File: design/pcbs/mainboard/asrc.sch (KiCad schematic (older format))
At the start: 18 parts, among them J5 Conn_01x03, U1 TPS79318-EP, U2 SRC4392

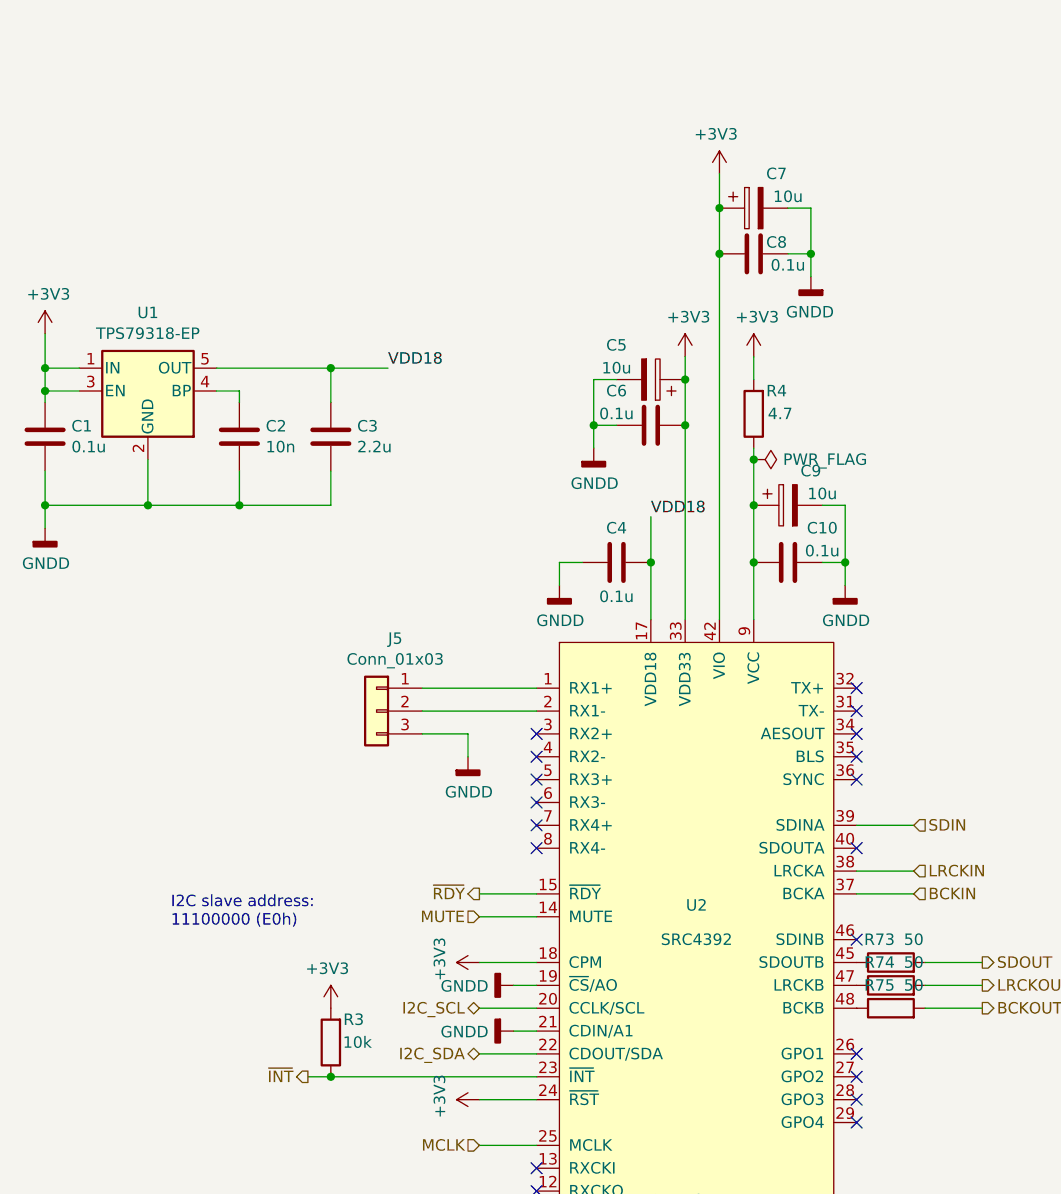
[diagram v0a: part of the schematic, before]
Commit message: Renumbered footprints to follow board position.
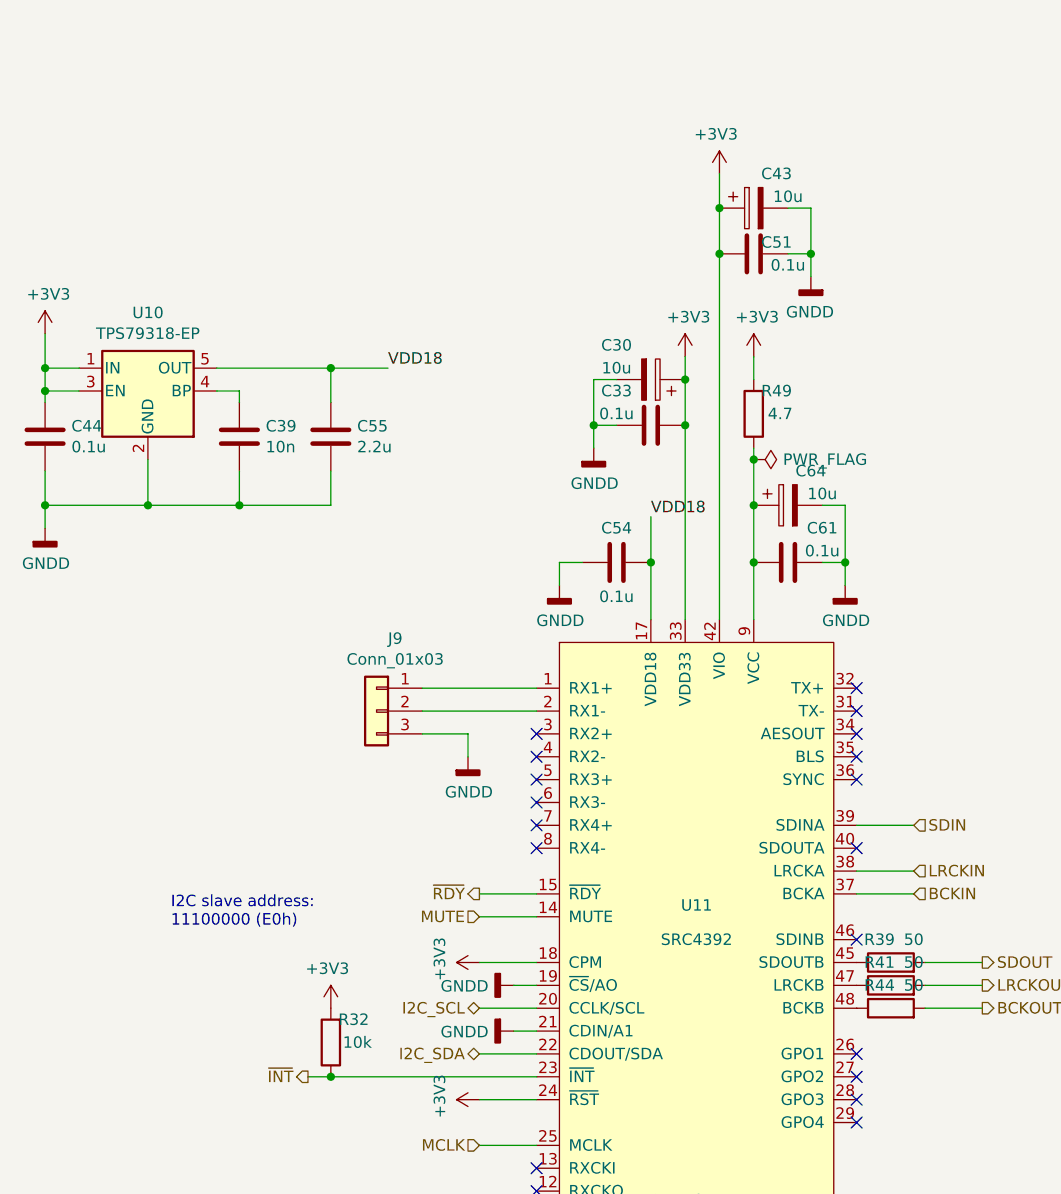
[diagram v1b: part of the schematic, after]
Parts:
- renumbered C5 to C30, C6 to C33, C2 to C39, C7 to C43, C1 to C44, C8 to C51, C4 to C54, C3 to C55, C10 to C61, C9 to C64, J5 to J9, R3 to R32, R73 to R39, R74 to R41, R75 to R44, R4 to R49, U1 to U10, U2 to U11
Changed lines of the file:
@@
 $EndDescr
 $Comp
-L dac:SRC4392 U2
+L dac:SRC4392 U11
 U 1 1 5EC7924C
 P 4700 4750
-F 0 "U2" H 4700 4900 50  0000 C CNN
+F 0 "U11" H 4700 4900 50  0000 C CNN
 F 1 "SRC4392" H 4700 4750 50  0000 C CNN
 F 2 "Package_QFP:TQFP-48_7x7mm_P0.5mm" H 4750 6100 50  0001 C CNN
@@
 $EndBitmap
 $Comp
-L Regulator_Linear:TPS79318-EP U1
+L Regulator_Linear:TPS79318-EP U10
 U 1 1 5EC6440E
 P 2300 2350
-F 0 "U1" H 2300 2692 50  0000 C CNN
+F 0 "U10" H 2300 2692 50  0000 C CNN
 F 1 "TPS79318-EP" H 2300 2601 50  0000 C CNN
 F 2 "Package_TO_SOT_SMD:SOT-23-5" H 2300 2675 50  0001 C CIN
@@
 $EndComp
 $Comp
-L Device:C C1
+L Device:C C44
 U 1 1 5EC64F1A
 P 1850 2550
-F 0 "C1" H 1965 2596 50  0000 L CNN
+F 0 "C44" H 1965 2596 50  0000 L CNN
 F 1 "0.1u" H 1965 2505 50  0000 L CNN
 F 2 "Capacitor_SMD:C_0603_1608Metric" H 1888 2400 50  0001 C CNN
@@
 $EndComp
 $Comp
-L Device:C C2
+L Device:C C39
 U 1 1 5EC677C7
 P 2700 2550
-F 0 "C2" H 2815 2596 50  0000 L CNN
+F 0 "C39" H 2815 2596 50  0000 L CNN
 F 1 "10n" H 2815 2505 50  0000 L CNN
 F 2 "Capacitor_SMD:C_0402_1005Metric" H 2738 2400 50  0001 C CNN
@@
 $EndComp
 $Comp
-L Device:C C3
+L Device:C C55
 U 1 1 5EC680BF
 P 3100 2550
-F 0 "C3" H 3215 2596 50  0000 L CNN
+F 0 "C55" H 3215 2596 50  0000 L CNN
 F 1 "2.2u" H 3215 2505 50  0000 L CNN
 F 2 "Capacitor_SMD:C_0603_1608Metric" H 3138 2400 50  0001 C CNN
@@
 Connection ~ 1850 2250
 $Comp
-L Device:C C10
+L Device:C C61
 U 1 1 5EC754F8
 P 5100 3100
-F 0 "C10" V 4950 3250 50  0000 C CNN
+F 0 "C61" V 4950 3250 50  0000 C CNN
 F 1 "0.1u" V 5050 3250 50  0000 C CNN
 F 2 "Capacitor_SMD:C_0603_1608Metric" H 5138 2950 50  0001 C CNN
@@
 $EndComp
 $Comp
-L Device:C C4
+L Device:C C54
 U 1 1 5EC782F3
 P 4350 3100
-F 0 "C4" V 4200 3100 50  0000 C CNN
+F 0 "C54" V 4200 3100 50  0000 C CNN
 F 1 "0.1u" V 4500 3100 50  0000 C CNN
 F 2 "Capacitor_SMD:C_0603_1608Metric" H 4388 2950 50  0001 C CNN
@@
 $EndComp
 $Comp
-L Device:CP C7
+L Device:CP C43
 U 1 1 5EC93F8F
 P 4950 1550
-F 0 "C7" V 4800 1450 50  0000 C CNN
+F 0 "C43" V 4800 1450 50  0000 C CNN
 F 1 "10u" V 4900 1400 50  0000 C CNN
 F 2 "Capacitor_Tantalum_SMD:CP_EIA-3216-18_Kemet-A" H 4988 1400 50  0001 C CNN
@@
 	4800 1550 4800 1750
 $Comp
-L Device:C C8
+L Device:C C51
 U 1 1 5EC944E8
 P 4950 1750
-F 0 "C8" V 4900 1650 50  0000 C CNN
+F 0 "C51" V 4900 1650 50  0000 C CNN
 F 1 "0.1u" V 5000 1600 50  0000 C CNN
 F 2 "Capacitor_SMD:C_0603_1608Metric" H 4988 1600 50  0001 C CNN
@@
 	4650 3350 4650 2500
 $Comp
-L Device:C C6
+L Device:C C33
 U 1 1 5ECB3139
 P 4500 2500
-F 0 "C6" V 4350 2350 50  0000 C CNN
+F 0 "C33" V 4350 2350 50  0000 C CNN
 F 1 "0.1u" V 4450 2350 50  0000 C CNN
 F 2 "Capacitor_SMD:C_0603_1608Metric" H 4538 2350 50  0001 C CNN
@@
 	4650 2200 4650 2300
 $Comp
-L Device:CP C5
+L Device:CP C30
 U 1 1 5ECEFB6A
 P 4500 2300
-F 0 "C5" V 4650 2150 50  0000 C CNN
+F 0 "C30" V 4650 2150 50  0000 C CNN
 F 1 "10u" V 4550 2150 50  0000 C CNN
 F 2 "Capacitor_Tantalum_SMD:CP_EIA-3216-18_Kemet-A" H 4538 2150 50  0001 C CNN
@@
 	4650 2300 4650 2500
 $Comp
-L Device:CP C9
+L Device:CP C64
 U 1 1 5ECF148F
 P 5100 2850
-F 0 "C9" V 4950 2750 50  0000 C CNN
+F 0 "C64" V 4950 2750 50  0000 C CNN
 F 1 "10u" V 5050 2700 50  0000 C CNN
 F 2 "Capacitor_Tantalum_SMD:CP_EIA-3216-18_Kemet-A" H 5138 2700 50  0001 C CNN
@@
 P 3100 5200
 AR Path="/5ECDE056" Ref="R?"  Part="1"
-AR Path="/5EC77FFA/5ECDE056" Ref="R3"  Part="1"
-F 0 "R3" H 3000 5100 50  0000 C CNN
+AR Path="/5EC77FFA/5ECDE056" Ref="R32"  Part="1"
+F 0 "R32" H 3000 5100 50  0000 C CNN
 F 1 "10k" H 2984 5200 50  0000 C CNN
 F 2 "Resistor_SMD:R_0402_1005Metric" V 3030 5200 50  0001 C CNN
@@
 P 4950 2450
 AR Path="/5ED97A18" Ref="R?"  Part="1"
-AR Path="/5EC77FFA/5ED97A18" Ref="R4"  Part="1"
-F 0 "R4" H 4850 2350 50  0000 C CNN
+AR Path="/5EC77FFA/5ED97A18" Ref="R49"  Part="1"
+F 0 "R49" H 4850 2350 50  0000 C CNN
 F 1 "4.7" H 4834 2450 50  0000 C CNN
 F 2 "Resistor_SMD:R_0603_1608Metric" V 4880 2450 50  0001 C CNN
@@
 NoConn ~ 4000 4350
 $Comp
-L Connector_Generic:Conn_01x03 J5
+L Connector_Generic:Conn_01x03 J9
 U 1 1 5EDD40DB
 P 3300 3750
-F 0 "J5" H 3218 4067 50  0000 C CNN
+F 0 "J9" H 3218 4067 50  0000 C CNN
 F 1 "Conn_01x03" H 3218 3976 50  0000 C CNN
 F 2 "Connector_PinHeader_2.54mm:PinHeader_1x03_P2.54mm_Vertical" H 3300 3750 50  0001 C CNN
@@
 P 5550 4850
 AR Path="/5EEA869D" Ref="R?"  Part="1"
-AR Path="/5EC77FFA/5EEA869D" Ref="R73"  Part="1"
-F 0 "R73" V 5650 4900 50  0000 C CNN
+AR Path="/5EC77FFA/5EEA869D" Ref="R39"  Part="1"
+F 0 "R39" V 5650 4900 50  0000 C CNN
 F 1 "50" V 5650 4750 50  0000 C CNN
 F 2 "Resistor_SMD:R_0402_1005Metric" V 5480 4850 50  0001 C CNN
@@
 P 5550 4950
 AR Path="/5EEAFFEA" Ref="R?"  Part="1"
-AR Path="/5EC77FFA/5EEAFFEA" Ref="R74"  Part="1"
-F 0 "R74" V 5650 5000 50  0000 C CNN
+AR Path="/5EC77FFA/5EEAFFEA" Ref="R41"  Part="1"
+F 0 "R41" V 5650 5000 50  0000 C CNN
 F 1 "50" V 5650 4850 50  0000 C CNN
 F 2 "Resistor_SMD:R_0402_1005Metric" V 5480 4950 50  0001 C CNN
@@
 P 5550 5050
 AR Path="/5EEB02AB" Ref="R?"  Part="1"
-AR Path="/5EC77FFA/5EEB02AB" Ref="R75"  Part="1"
-F 0 "R75" V 5650 5100 50  0000 C CNN
+AR Path="/5EC77FFA/5EEB02AB" Ref="R44"  Part="1"
+F 0 "R44" V 5650 5100 50  0000 C CNN
 F 1 "50" V 5650 4950 50  0000 C CNN
 F 2 "Resistor_SMD:R_0402_1005Metric" V 5480 5050 50  0001 C CNN

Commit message: Fixed title blocks. Added fab outputs.
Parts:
- U10: LCSC (none) -> C7102
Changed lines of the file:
@@
 encoding utf-8
 Sheet 2 10
-Title ""
-Date ""
-Rev ""
-Comp ""
-Comment1 ""
-Comment2 ""
+Title "DAC1 Main board"
+Date "2020-06-27"
+Rev "1.0.0"
+Comp "© Mark Pinese 2020"
+Comment1 "To view a copy of this license, visit https://creativecommons.org/licenses/by/4.0"
+Comment2 "This work is licensed under CC BY 4.0."
 Comment3 ""
 Comment4 ""
@@
 F 4 "296-12155-1-ND" H 2300 2350 50  0001 C CNN "DigiKey"
 F 5 "Yes" H 2300 2350 50  0001 C CNN "Done"
+F 6 "C7102" H 2300 2350 50  0001 C CNN "LCSC"
 	1    2300 2350
 	1    0    0    -1

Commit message: Misc updates
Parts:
- R39, R41, R44: value 50 -> 10; LCSC C25082 -> C25077
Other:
- moved on the sheet: R39, R41, R44
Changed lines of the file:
@@
 $EndComp
 Wire Wire Line
-	5950 5050 5700 5050
+	6100 5050 5850 5050
 Wire Wire Line
-	5700 4950 5950 4950
-Text HLabel 5950 5050 2    50   Output ~ 0
+	5850 4950 6100 4950
+Text HLabel 6100 5050 2    50   Output ~ 0
 BCKOUT
-Text HLabel 5950 4950 2    50   Output ~ 0
+Text HLabel 6100 4950 2    50   Output ~ 0
 LRCKOUT
 Wire Wire Line
-	5700 4850 5950 4850
-Text HLabel 5950 4850 2    50   Output ~ 0
+	5850 4850 6100 4850
+Text HLabel 6100 4850 2    50   Output ~ 0
 SDOUT
 $Comp
 L Device:R R?
 U 1 1 5EEA869D
-P 5550 4850
+P 5700 4850
 AR Path="/5EEA869D" Ref="R?"  Part="1"
 AR Path="/5EC77FFA/5EEA869D" Ref="R39"  Part="1"
-F 0 "R39" V 5650 4900 50  0000 C CNN
-F 1 "50" V 5650 4750 50  0000 C CNN
-F 2 "Resistor_SMD:R_0402_1005Metric" V 5480 4850 50  0001 C CNN
-F 3 "https://datasheet.lcsc.com/szlcsc/Uniroyal-Elec-0402WGF1500TCE_C25082.pdf" H 5550 4850 50  0001 C CNN
-F 4 "C25082" H 5550 4850 50  0001 C CNN "LCSC"
-F 5 "Yes" H 5550 4850 50  0001 C CNN "Done"
-F 6 "Termination" H 5550 4850 50  0001 C CNN "Function"
-	1    5550 4850
+F 0 "R39" V 5750 5050 50  0000 C CNN
+F 1 "10" V 5700 4850 50  0000 C CNN
+F 2 "Resistor_SMD:R_0402_1005Metric" V 5630 4850 50  0001 C CNN
+F 3 "Uniroyal-Elec-0402WGF100JTCE_C25077.pdf" H 5700 4850 50  0001 C CNN
+F 4 "C25077" H 5700 4850 50  0001 C CNN "LCSC"
+F 5 "Yes" H 5700 4850 50  0001 C CNN "Done"
+F 6 "Termination" H 5700 4850 50  0001 C CNN "Function"
+	1    5700 4850
 	0    -1   -1   0
 $EndComp
@@
 L Device:R R?
 U 1 1 5EEAFFEA
-P 5550 4950
+P 5700 4950
 AR Path="/5EEAFFEA" Ref="R?"  Part="1"
 AR Path="/5EC77FFA/5EEAFFEA" Ref="R41"  Part="1"
-F 0 "R41" V 5650 5000 50  0000 C CNN
-F 1 "50" V 5650 4850 50  0000 C CNN
-F 2 "Resistor_SMD:R_0402_1005Metric" V 5480 4950 50  0001 C CNN
-F 3 "https://datasheet.lcsc.com/szlcsc/Uniroyal-Elec-0402WGF1500TCE_C25082.pdf" H 5550 4950 50  0001 C CNN
-F 4 "C25082" H 5550 4950 50  0001 C CNN "LCSC"
-F 5 "Yes" H 5550 4950 50  0001 C CNN "Done"
-F 6 "Termination" H 5550 4950 50  0001 C CNN "Function"
-	1    5550 4950
+F 0 "R41" V 5750 5150 50  0000 C CNN
+F 1 "10" V 5700 4950 50  0000 C CNN
+F 2 "Resistor_SMD:R_0402_1005Metric" V 5630 4950 50  0001 C CNN
+F 3 "Uniroyal-Elec-0402WGF100JTCE_C25077.pdf" H 5700 4950 50  0001 C CNN
+F 4 "C25077" H 5700 4950 50  0001 C CNN "LCSC"
+F 5 "Yes" H 5700 4950 50  0001 C CNN "Done"
+F 6 "Termination" H 5700 4950 50  0001 C CNN "Function"
+	1    5700 4950
 	0    -1   -1   0
 $EndComp
@@
 L Device:R R?
 U 1 1 5EEB02AB
-P 5550 5050
+P 5700 5050
 AR Path="/5EEB02AB" Ref="R?"  Part="1"
 AR Path="/5EC77FFA/5EEB02AB" Ref="R44"  Part="1"
-F 0 "R44" V 5650 5100 50  0000 C CNN
-F 1 "50" V 5650 4950 50  0000 C CNN
-F 2 "Resistor_SMD:R_0402_1005Metric" V 5480 5050 50  0001 C CNN
-F 3 "https://datasheet.lcsc.com/szlcsc/Uniroyal-Elec-0402WGF1500TCE_C25082.pdf" H 5550 5050 50  0001 C CNN
-F 4 "C25082" H 5550 5050 50  0001 C CNN "LCSC"
-F 5 "Yes" H 5550 5050 50  0001 C CNN "Done"
-F 6 "Termination" H 5550 5050 50  0001 C CNN "Function"
-	1    5550 5050
+F 0 "R44" V 5750 5250 50  0000 C CNN
+F 1 "10" V 5700 5050 50  0000 C CNN
+F 2 "Resistor_SMD:R_0402_1005Metric" V 5630 5050 50  0001 C CNN
+F 3 "Uniroyal-Elec-0402WGF100JTCE_C25077.pdf" H 5700 5050 50  0001 C CNN
+F 4 "C25077" H 5700 5050 50  0001 C CNN "LCSC"
+F 5 "Yes" H 5700 5050 50  0001 C CNN "Done"
+F 6 "Termination" H 5700 5050 50  0001 C CNN "Function"
+	1    5700 5050
 	0    -1   -1   0
 $EndComp
+Wire Wire Line
+	5550 4850 5400 4850
+Wire Wire Line
+	5400 5050 5550 5050
+Wire Wire Line
+	5550 4950 5400 4950
 $EndSCHEMATC
